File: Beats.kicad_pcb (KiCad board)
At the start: 4 copper layers, 60 x 106.5 mm, 123 parts, among them J1 AudioJack2_SwitchT, J10 AudioJack2_SwitchT, J11 AudioJack2_SwitchT, J12 AudioJack2_SwitchT, J13 AudioJack2_SwitchT, J14 AudioJack2_SwitchT, J15 AudioJack2_SwitchT, J16 AudioJack2_SwitchT, J17 Conn_02x05_Odd_Even, J18 UART, J2 AudioJack2_SwitchT, J3 AudioJack2_SwitchT, J4 AudioJack2_SwitchT, J5 AudioJack2_SwitchT, J6 AudioJack2_SwitchT, J7 SWD, J8 Conn_01x03_Male, J9 AudioJack2_SwitchT, Q1 BC847, Q10 BC847, Q11 BC847, Q12 BC847, Q13 BC847, Q14 BC847, Q15 BC847, Q2 BC847, Q3 BC847, Q4 BC847, Q5 BC847, Q6 BC847, Q7 BC847, Q8 BC847, Q9 BC847, SW1 Rotary_Encoder_Switch, SW10 SW_Push_LED, SW11 SW_Push_LED, SW12 SW_Push_LED, SW13 SW_Push_LED, SW2 SW_Push, SW3 SW_Push_LED, SW4 SW_Push_LED, SW5 SW_Push_LED, SW6 SW_Push_LED, SW7 SW_Push_LED, SW8 SW_Push_LED, SW9 SW_Push_LED, U1 MCP6004, U2 IPS240x240, U3 STM32F051R8Tx, U4 AT25xxx, U5 74AHCT244, U6 L7805, U7 LM1117-3.3, Y1 8MHz

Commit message: Branding and legends.
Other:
- board text added: "+12V"
- board text added: "-12V"
- board text added: "BOOT"
- board text added: "Beats"
- board text added: "Marangisto 2019"
- board text added: "Rev A"
- board text added: "SWD"
- board text added: "UART"
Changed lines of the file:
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@@
   (general
     (thickness 1.6)
-    (drawings 91)
+    (drawings 100)
     (tracks 101)
     (zones 0)
@@
     (descr "Through hole straight pin header, 2x05, 2.54mm pitch, double rows")
     (tags "Through hole pin header THT 2x05 2.54mm double row")
-    (fp_text reference J17 (at 1.27 2.33) (layer B.SilkS)
+    (fp_text reference J17 (at 0.508 -14.224) (layer B.SilkS)
       (effects (font (size 1 1) (thickness 0.15)) (justify mirror))
     )
@@
     )
   )
+  (gr_text -12V (at 124.346 125.4) (layer B.SilkS)
+    (effects (font (size 1 1) (thickness 0.15)) (justify mirror))
+  )
+  (gr_line (start 126.505 124.13) (end 121.298 124.13) (layer B.SilkS) (width 0.4))
+  (gr_text +12V (at 123.965 109.652) (layer B.SilkS)
+    (effects (font (size 1 1) (thickness 0.15)) (justify mirror))
+  )
+  (gr_text "Rev A" (at 177.686 148.514 90) (layer B.SilkS)
+    (effects (font (size 1.5 1.5) (thickness 0.15)) (justify mirror))
+  )
+  (gr_text "Marangisto 2019" (at 122.441 142.164 90) (layer B.SilkS)
+    (effects (font (size 1.5 1.5) (thickness 0.15)) (justify mirror))
+  )
+  (gr_text Beats (at 155.334 63.17 90) (layer B.SilkS)
+    (effects (font (size 4 6) (thickness 0.5)) (justify mirror))
+  )
+  (gr_text BOOT (at 128.537 68.123) (layer B.SilkS)
+    (effects (font (size 1 1) (thickness 0.15)) (justify mirror))
+  )
+  (gr_text UART (at 122.695 90.856) (layer B.SilkS)
+    (effects (font (size 1 1) (thickness 0.15)) (justify mirror))
+  )
+  (gr_text "SWD\n" (at 122.695 71.806) (layer B.SilkS)
+    (effects (font (size 1 1) (thickness 0.15)) (justify mirror))
+  )
   (dimension 59.959999 (width 0.15) (layer Dwgs.User)

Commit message: Pin assingment for input clock and reset signals.
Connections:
- Q1 pad 3: /DigitalIn/Trig -> PB7
- Q2 pad 3: /sheet5D7C6377/Trig -> PD2
- R27 pad 2: /DigitalIn/Trig -> PB7
- R29 pad 2: /sheet5D7C6377/Trig -> PD2
- U2 pad 7: PD2 -> +3.3VA
- U4 pad 7: PB7 -> +3.3VA

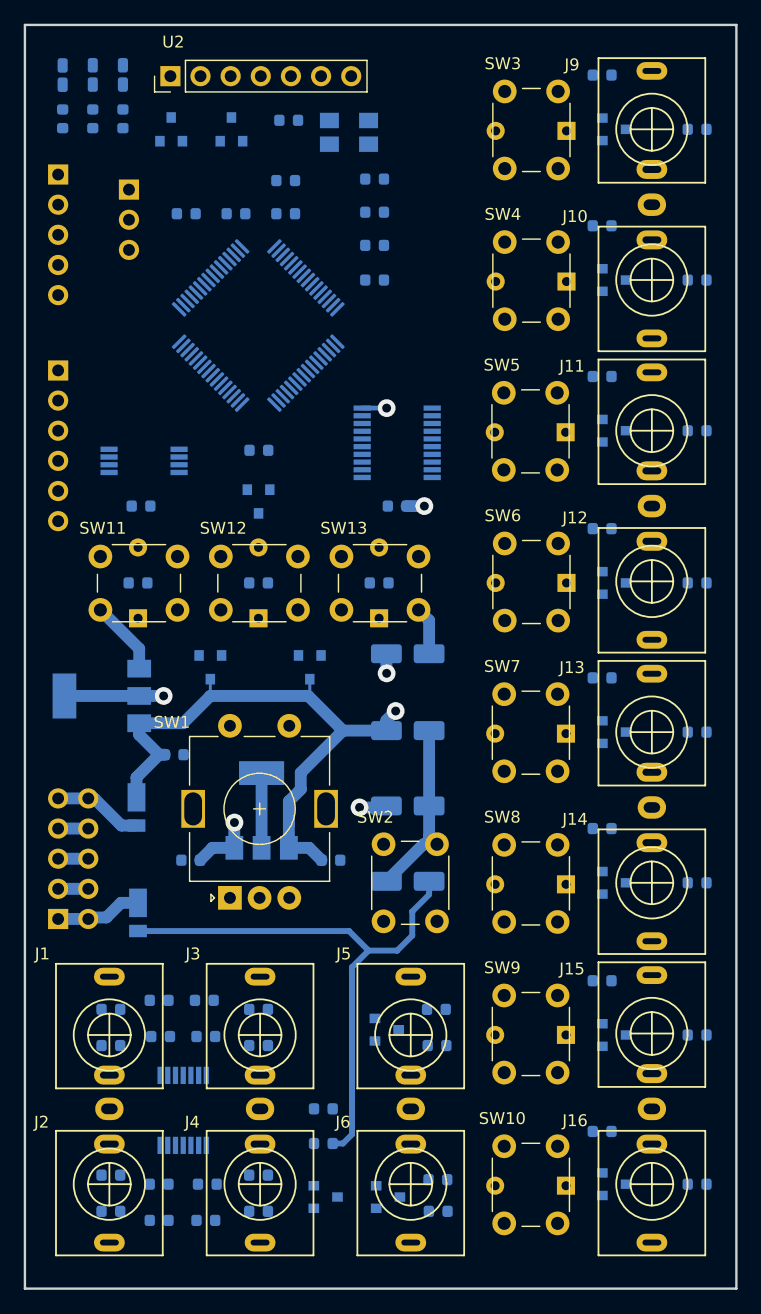
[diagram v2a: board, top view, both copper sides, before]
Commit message: Free-routed signals.
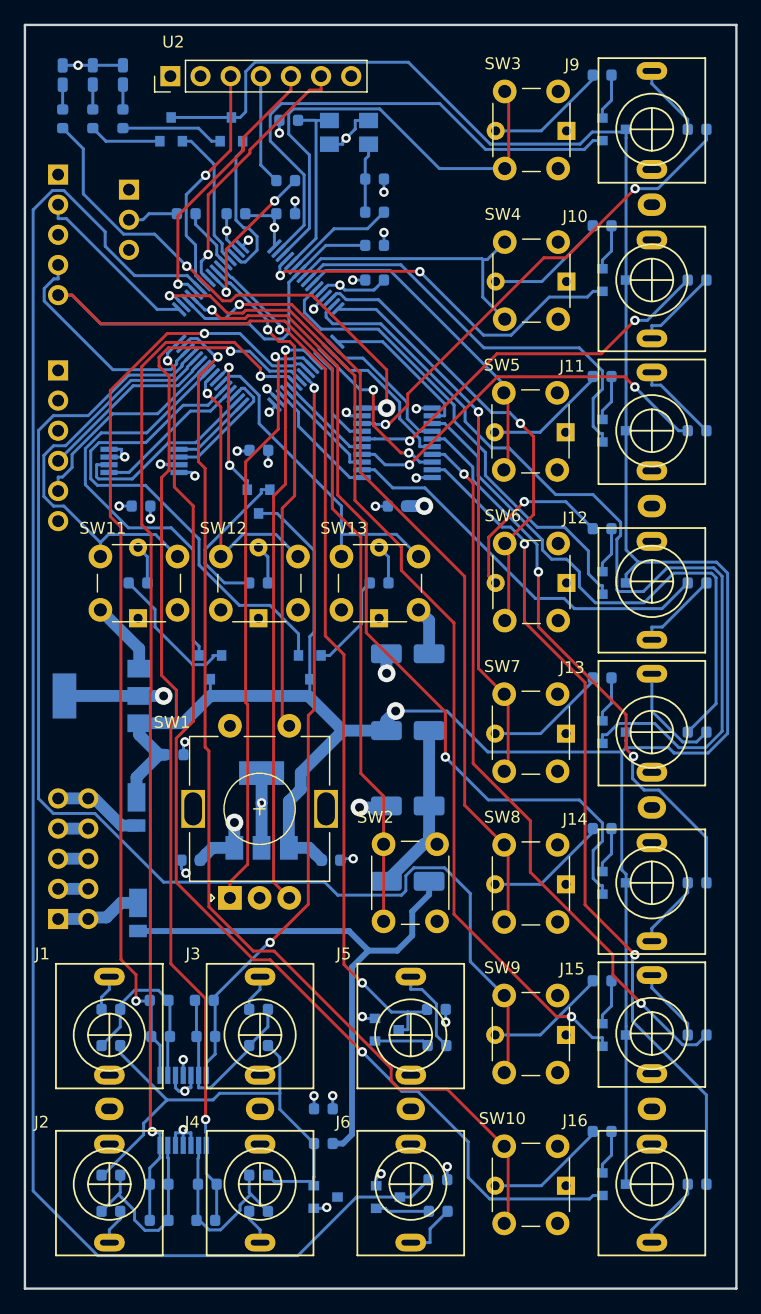
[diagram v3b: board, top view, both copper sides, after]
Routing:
- net +12V: track 207.1 -> 399.1 mm
- net PD2: track 0.00 -> 139.8 mm
- net RESET: track 0.00 -> 107.4 mm
- net PA12: track 0.00 -> 105.6 mm
- net PF7: track 0.00 -> 96.3 mm, vias 0 -> 2
- net PF6: track 0.00 -> 91.9 mm, vias 0 -> 1
- net PB0: track 0.00 -> 89.0 mm, vias 0 -> 2
- net PB1: track 0.00 -> 88.9 mm, vias 0 -> 2
- net PA15: track 0.00 -> 86.5 mm, vias 0 -> 2
- net PC4: track 0.00 -> 80.3 mm, vias 0 -> 2
- net PA1: track 0.00 -> 75.5 mm
- net PB7: track 0.00 -> 74.4 mm, vias 0 -> 2
- net PC11: track 0.00 -> 73.9 mm, vias 0 -> 2
- net Net-(R23-Pad2): track 0.00 -> 71.0 mm, vias 0 -> 2
- net PC10: track 0.00 -> 69.6 mm, vias 0 -> 1
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
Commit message: Stitching of head-sinks for 3.3V.
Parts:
- moved R2 0.25 mm to (127.1, 130.0)
- moved R4 0.25 mm to (139.6, 130.0)
- moved R5 0.25 mm to (139.6, 143.9)
- moved R7 0.25 mm to (127.1, 143.9)
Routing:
- net +3.3VA: vias 15 -> 48
- added copper zone on B.Cu, net +3.3VA
- added copper zone on F.Cu, net +3.3VA
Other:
- board text removed: "+12V"

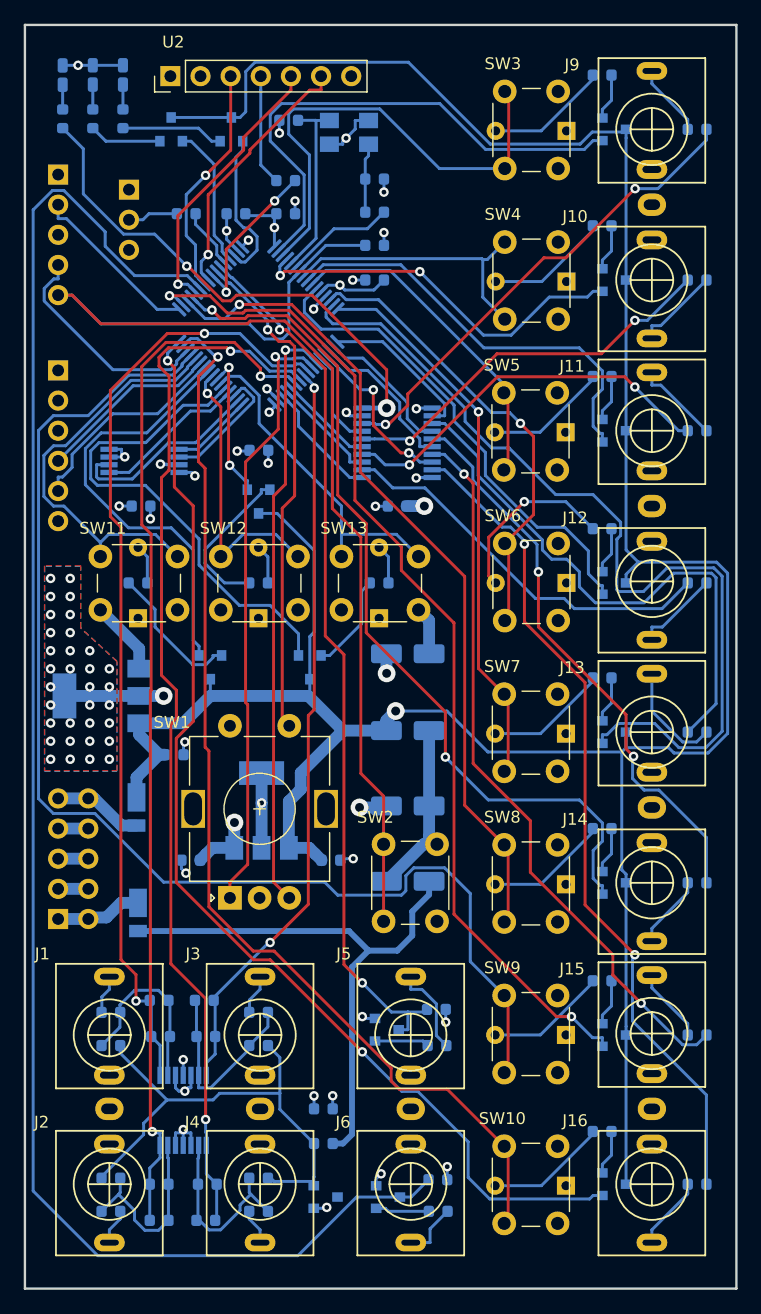
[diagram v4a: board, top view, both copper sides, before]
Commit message: Revised chip power connections.
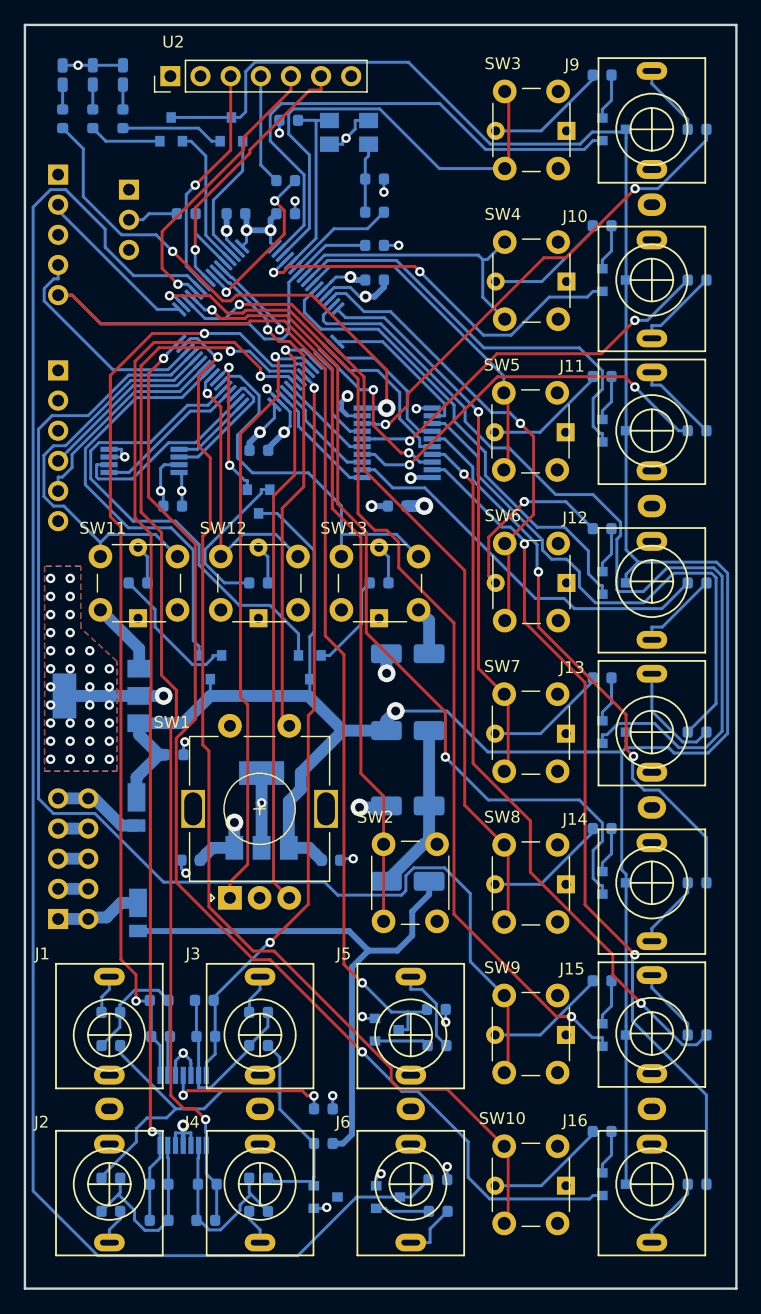
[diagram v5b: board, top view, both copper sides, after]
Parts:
- moved C13 2.67 mm to (132.3, 87.3)
- turned C12 to 180 degrees
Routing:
- net +3.3VA: track 30.8 -> 54.2 mm, vias 48 -> 45
- net GND: track 90.2 -> 98.5 mm, vias 26 -> 25
- net PC7: track 27.8 -> 32.1 mm
- net PB0: track 89.0 -> 90.7 mm
- net PB9: track 13.0 -> 11.3 mm
- net PF7: track 96.3 -> 97.8 mm
- net VRef-10: track 42.6 -> 43.9 mm
- net PC12: track 23.3 -> 24.4 mm
- net PB1: track 88.9 -> 90.0 mm
- net PC15: track 32.7 -> 33.4 mm
- net PC4: track 80.3 -> 81.0 mm
- net PC2: track 28.1 -> 28.8 mm
- net PB5: track 13.7 -> 14.3 mm
- net PA6: track 50.2 -> 50.8 mm
- net PB6: track 42.3 -> 42.9 mm
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
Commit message: Pours on top and bottom layers.
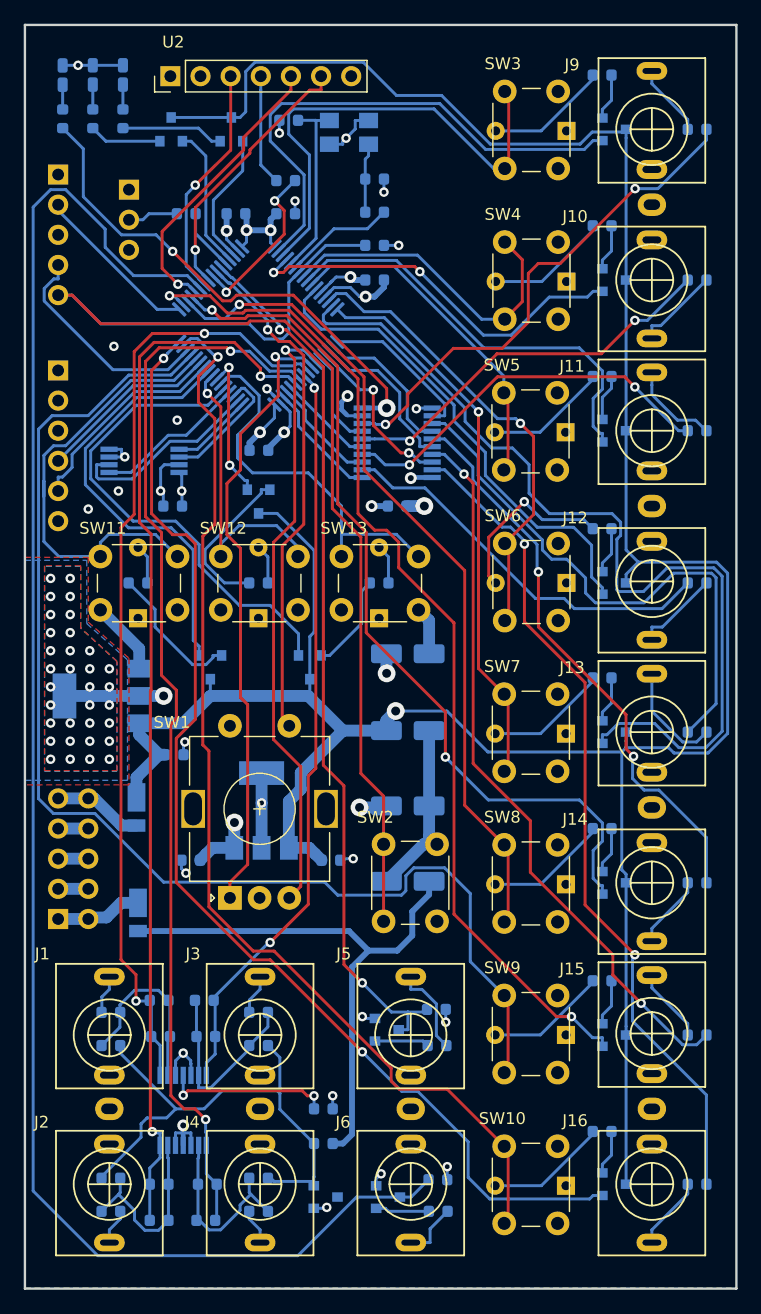
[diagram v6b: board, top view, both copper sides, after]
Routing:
- net PA11: track 34.8 -> 38.8 mm
- net PC0: track 24.2 -> 27.6 mm
- net Net-(R16-Pad2): track 40.4 -> 42.9 mm
- net PC9: track 24.1 -> 25.8 mm
- net PA1: track 76.0 -> 77.4 mm
- net PA7: track 51.4 -> 52.4 mm
- net +5V: track 110.4 -> 109.5 mm
- net PA6: track 50.8 -> 51.6 mm
- net PC4: track 81.0 -> 80.3 mm
- net GND: vias 25 -> 29
- added copper zone on B.Cu, net GND
- added copper zone on F.Cu, net GND
